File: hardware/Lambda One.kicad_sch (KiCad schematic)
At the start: 20 parts, among them IC1 01, J1 Conn_01x02, SW1 SW_Push, U1 W65C816SxP, U3 ATF22V10C, U6 74AHC1G04, Y1 TFT680

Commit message: Fixed some erros, changed to 3V
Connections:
- net +3.3V: now also IC1.2 (VCC), J1.2 (Pin_2), U1.8 (VDD), U3.24 (VCC), Y1.14 (Vcc)
- net +5V: no longer IC1.2 (VCC), J1.2 (Pin_2), U1.8 (VDD), U3.24 (VCC), Y1.14 (Vcc)

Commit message: Fixed all erros and warning
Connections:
- net +5V is gone; now on net +3.3V: R17.2, Y1.1 (EN)
- net IRQ_{1} renamed ~{IRQ}

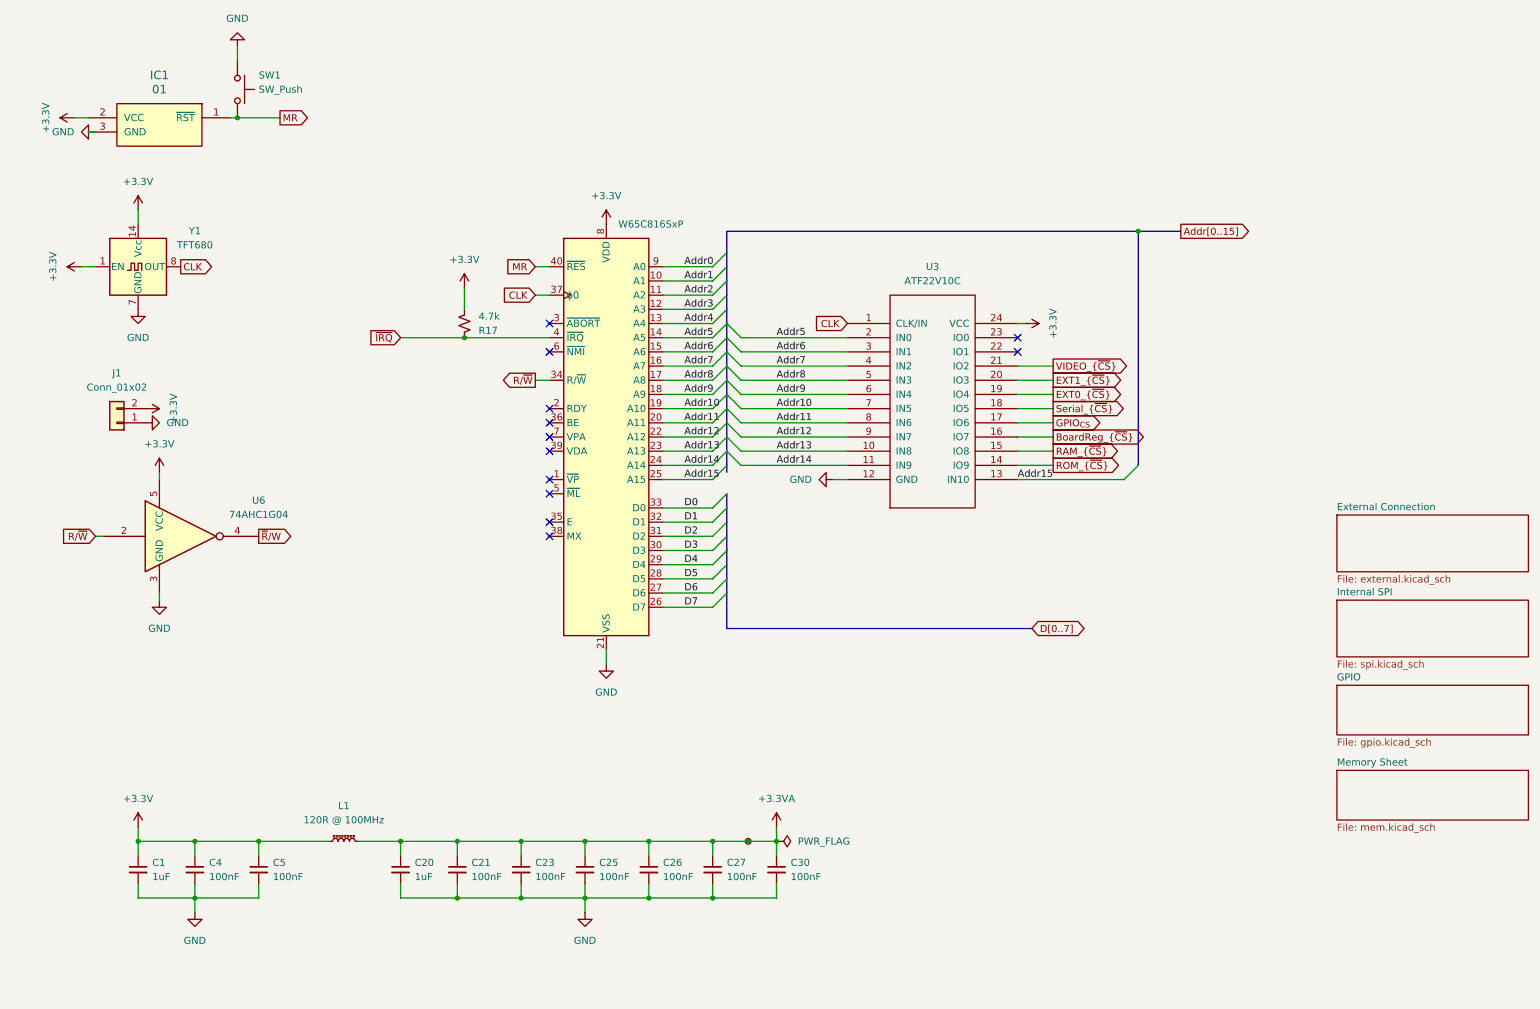
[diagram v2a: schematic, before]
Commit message: Fixed critical bugs on the system related to memory maping and IC selections
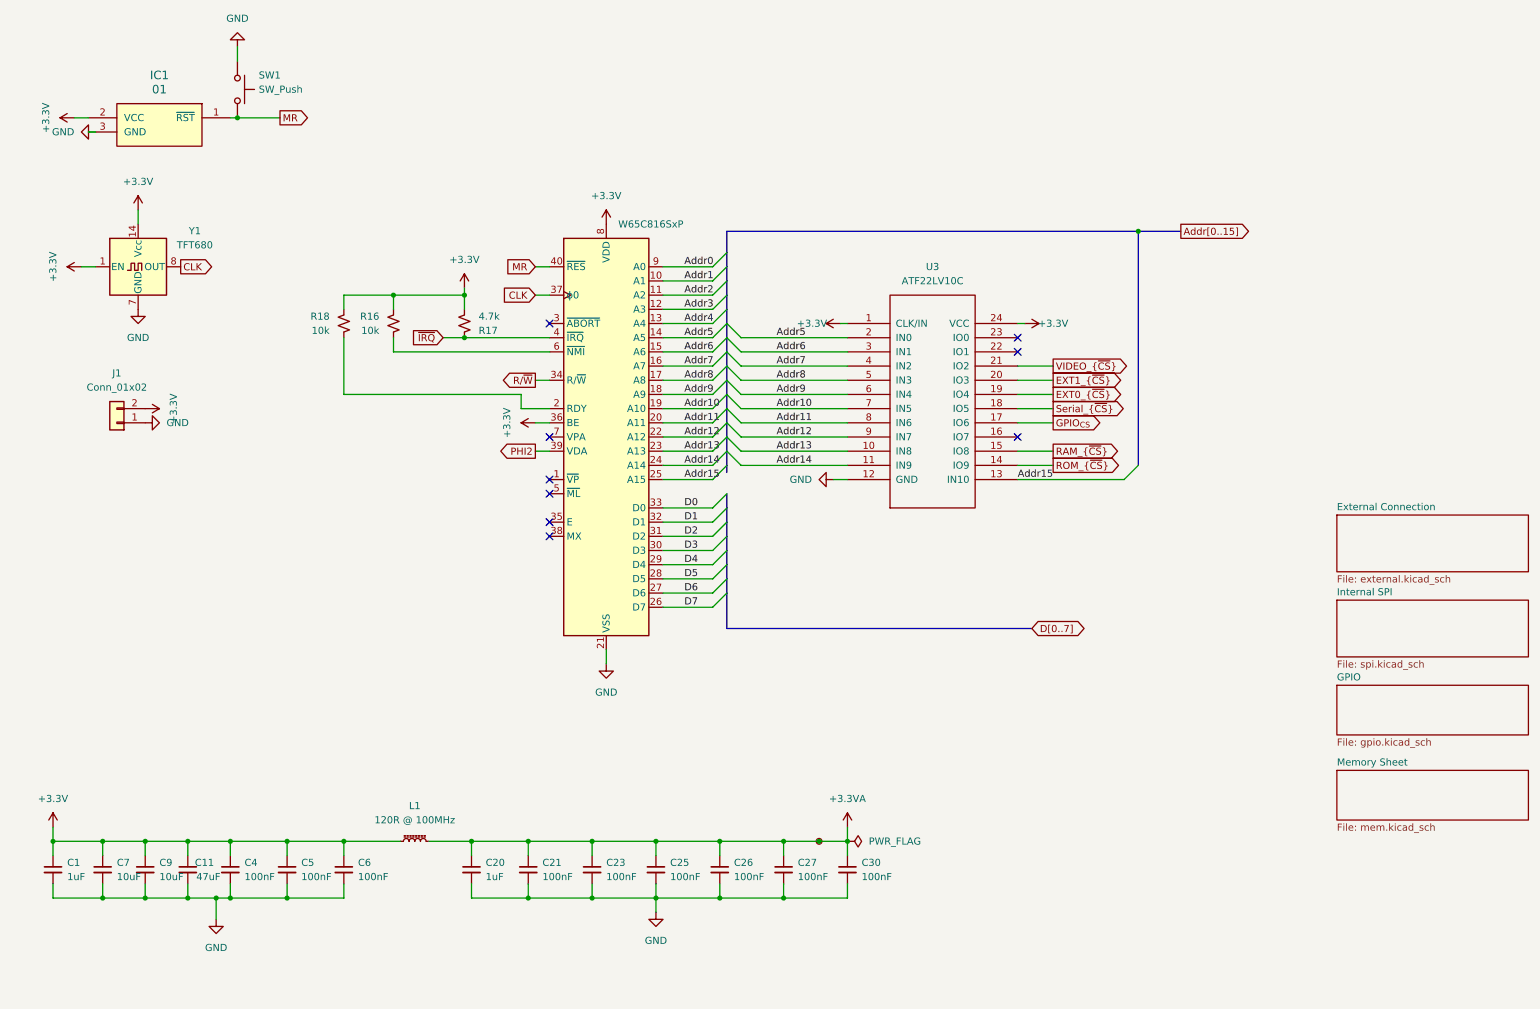
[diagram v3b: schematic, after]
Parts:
- removed U6: 74AHC1G04, Package_TO_SOT_SMD:SOT-23-5, symbol 74xGxx:74AHC1G04
- added C11: 47uF, Capacitor_SMD:C_0603_1608Metric, symbol Device:C_Small
- added C6: 100nF, Capacitor_SMD:C_0603_1608Metric, symbol Device:C_Small
- added C7, C9: 10uF, Capacitor_SMD:C_0603_1608Metric, symbol Device:C_Small
- added R16, R18: 10k, Resistor_SMD:R_0603_1608Metric, symbol Device:R_Small_US
- U3: value ATF22V10C -> ATF22LV10C
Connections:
- net +3.3V: now also U1.36 (BE), U3.1 (CLK/IN), C11.1, C6.1, C7.1, C9.1, R16.1, R18.1
- net CLK: no longer U3.1 (CLK/IN)
- net GND: now also C11.2, C6.2, C7.2, C9.2
- net at U1.2 (RDY): now also R18.2
- net PHI2: now reaches U1.39 (VDA)
- net at U1.6 (~{NMI}): now also R16.2
- net BoardReg_{~{CS}}: no longer names the net of U3.16 (IO7)
- no-connect marks 12 -> 9
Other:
- moved on the sheet: C1, C20, C21, C23, C25, C26, C27, C30, C4, C5, L1

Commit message: Changed Ethernet Chip to Ethernet ModuleWIZ850IO
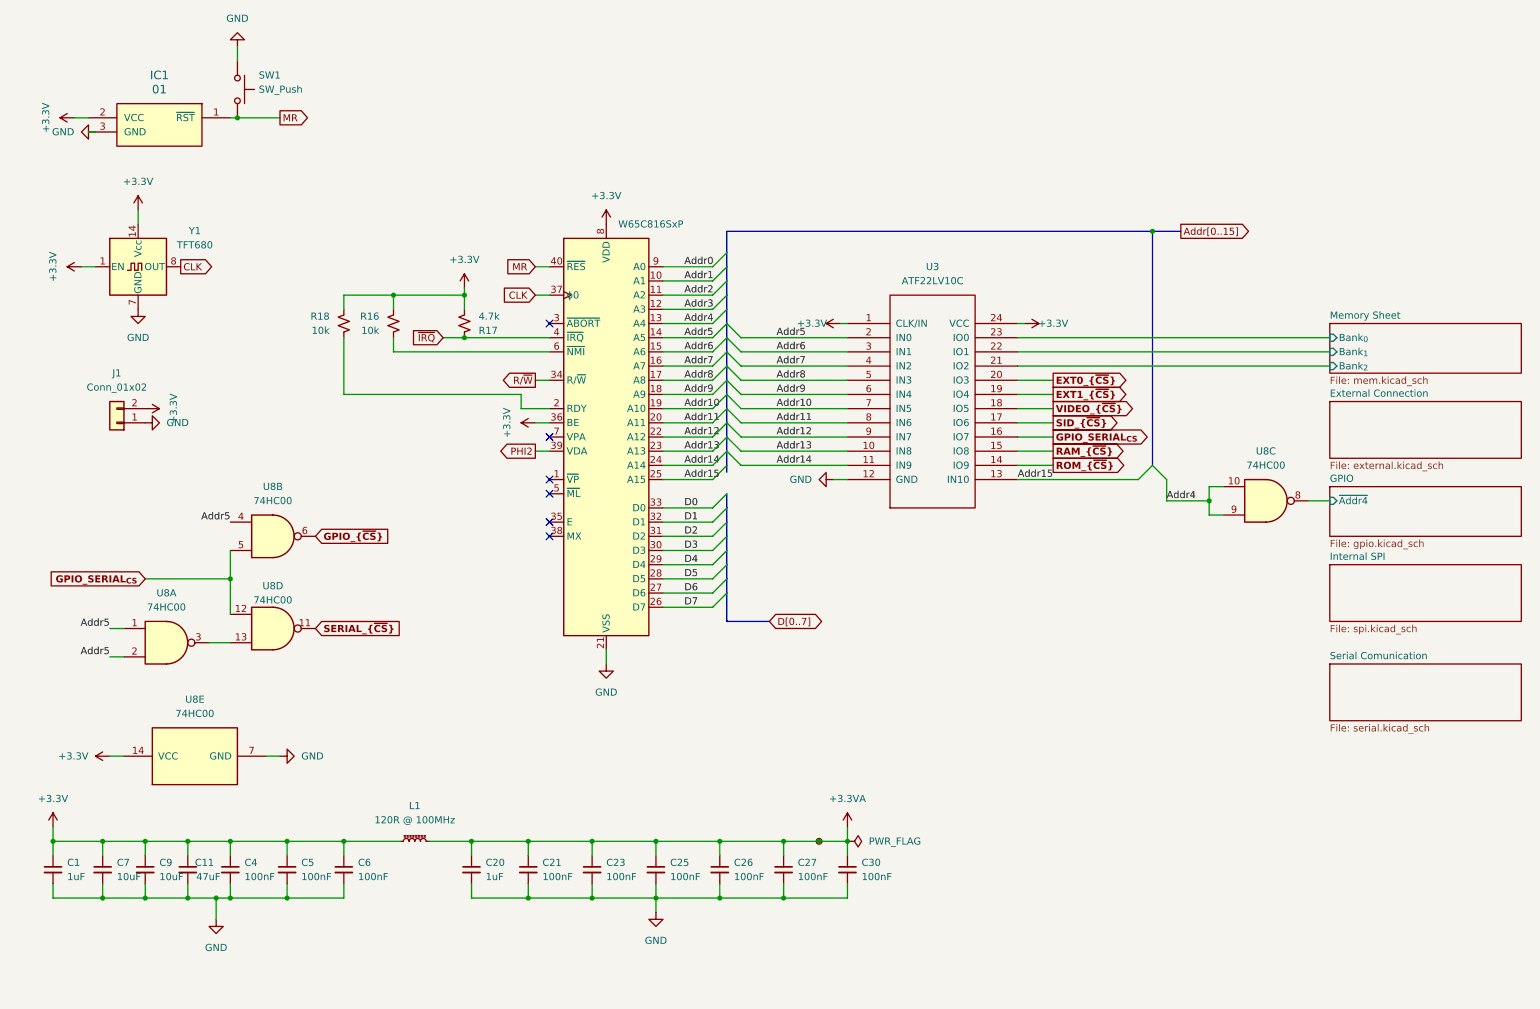
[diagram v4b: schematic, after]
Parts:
- added U8: 74HC00, symbol 74xx:74HC00
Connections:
- net Serial_{~{CS}} is gone; now on net VIDEO_{~{CS}}: U3.18 (IO5)
- net +3.3V: now also U8.14 (VCC)
- net Addr4: now also U8.10, U8.9
- net Addr5: now also U8.1, U8.2, U8.4
- net EXT0_{~{CS}}: now also U3.20 (IO3); no longer U3.19 (IO4)
- net EXT1_{~{CS}}: now also U3.19 (IO4); no longer U3.20 (IO3)
- net GND: now also U8.7 (GND)
- net VIDEO_{~{CS}}: no longer U3.21 (IO2)
- net GPIO_SERIAL_{CS}: now reaches U3.16 (IO7)
- net GPIO_SERIAL_{CS}: now also U8.12, U8.5
- net Memory Sheet/Bank_{1}: now reaches U3.22 (IO1)
- net Memory Sheet/Bank_{0}: now reaches U3.23 (IO0)
- net GPIO_{CS} renamed SID_{~{CS}}
- new net: U8.13, U8.3
- new net GPIO/~{Addr4}: U8.8
- new net GPIO_{~{CS}}: U8.6
- new net Memory Sheet/Bank_{2}: U3.21 (IO2)
- new net SERIAL_{~{CS}}: U8.11
- no-connect marks 9 -> 6
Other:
- added sheet Serial Comunication (serial.kicad_sch)
- sheet GPIO ports: added ~{Addr4}; removed none
- sheet Memory Sheet ports: added Bank_{0}, Bank_{1}, Bank_{2}; removed none

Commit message: Fixes and addres fix adding VDA AND VPA
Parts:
- removed C26, C27, C30: 100nF, Capacitor_SMD:C_0603_1608Metric, symbol Device:C_Small
- removed L1: 120R @ 100MHz, Inductor_SMD:L_0603_1608Metric, symbol Device:L_Ferrite_Small
- removed TP13: TestPoint_Small, TestPoint:TestPoint_Pad_D1.5mm, symbol Connector:TestPoint_Small
- added C2: 47uF, Capacitor_SMD:C_0603_1608Metric, symbol Device:C_Small
- added U9: 74HC00, symbol 74xx:74HC00
- IC1: value 01 -> DS1818
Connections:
- net +3.3VA is gone; now on net +3.3V: C20.1, C21.1, C23.1, C25.1
- net +3.3V: now also C2.1, U9.14 (VCC); no longer U3.1 (CLK/IN)
- net GND: now also C2.2, U9.7 (GND)
- net at U1.7 (VPA): now also U9.1, U9.2
- net PHI2: no longer names the net of U1.39 (VDA)
- net PHI2: now also U9.10, U9.9
- new net: U9.4, U9.8
- new net: U9.3, U9.5
- new net VDA&VPA: U3.1 (CLK/IN), U9.6
- no-connect marks 6 -> 8
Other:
- moved on the sheet: C1, C11, C20, C21, C23, C25, C4, C5, C6, C7, C9, R16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

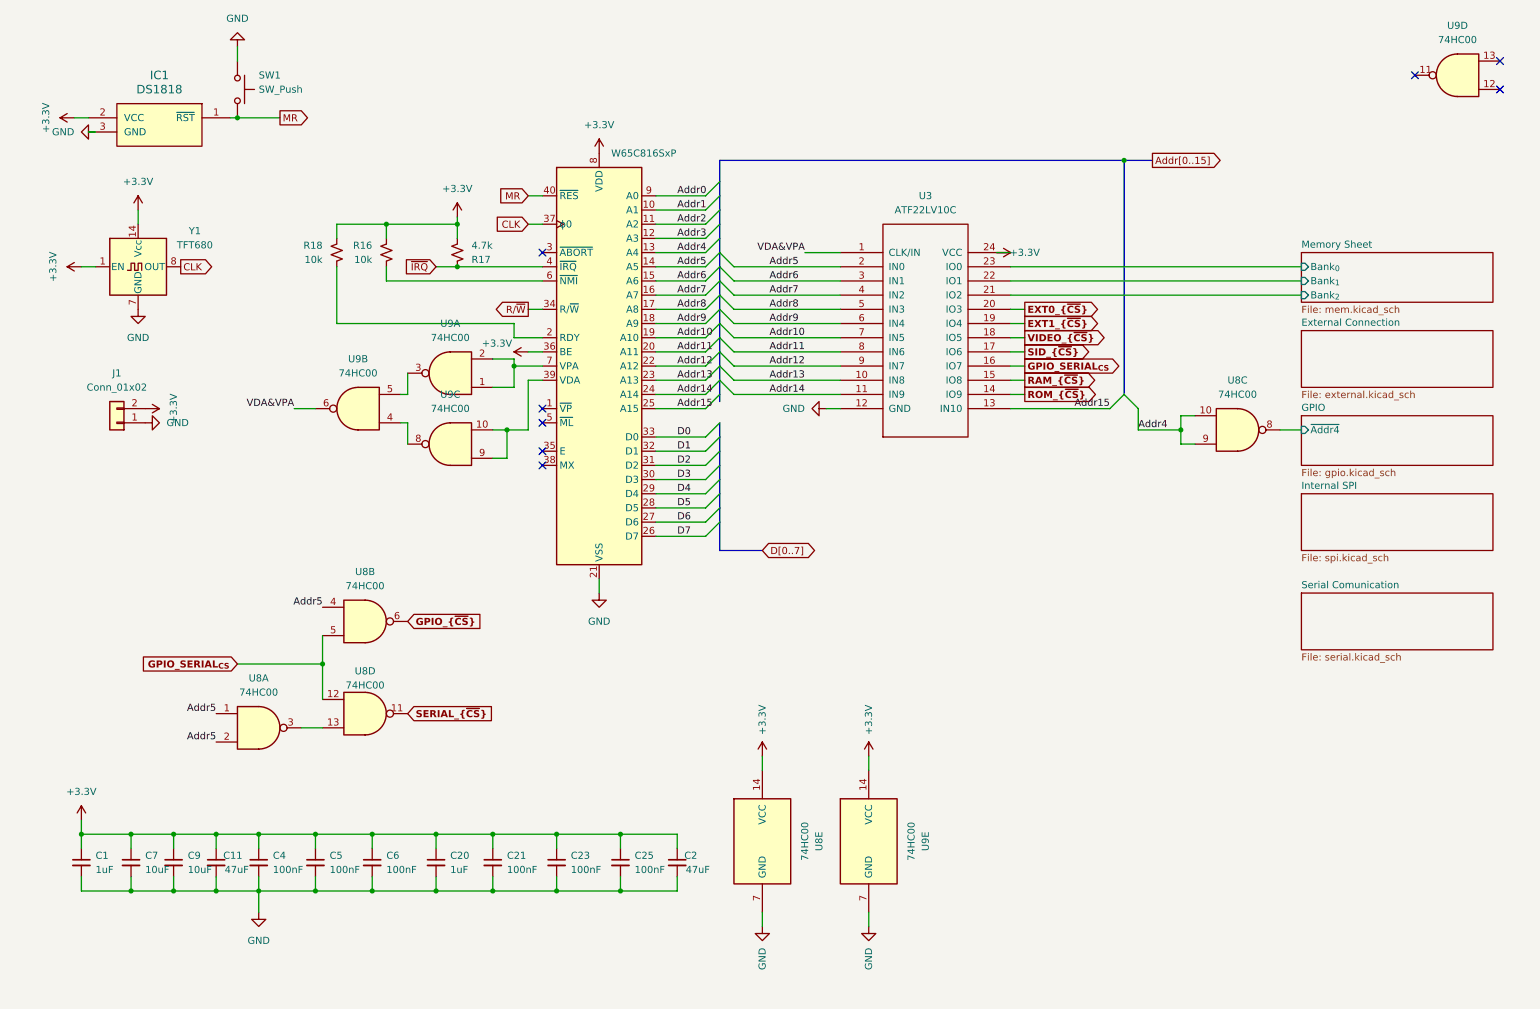
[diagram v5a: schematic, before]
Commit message: Added Bus controller 74HC245
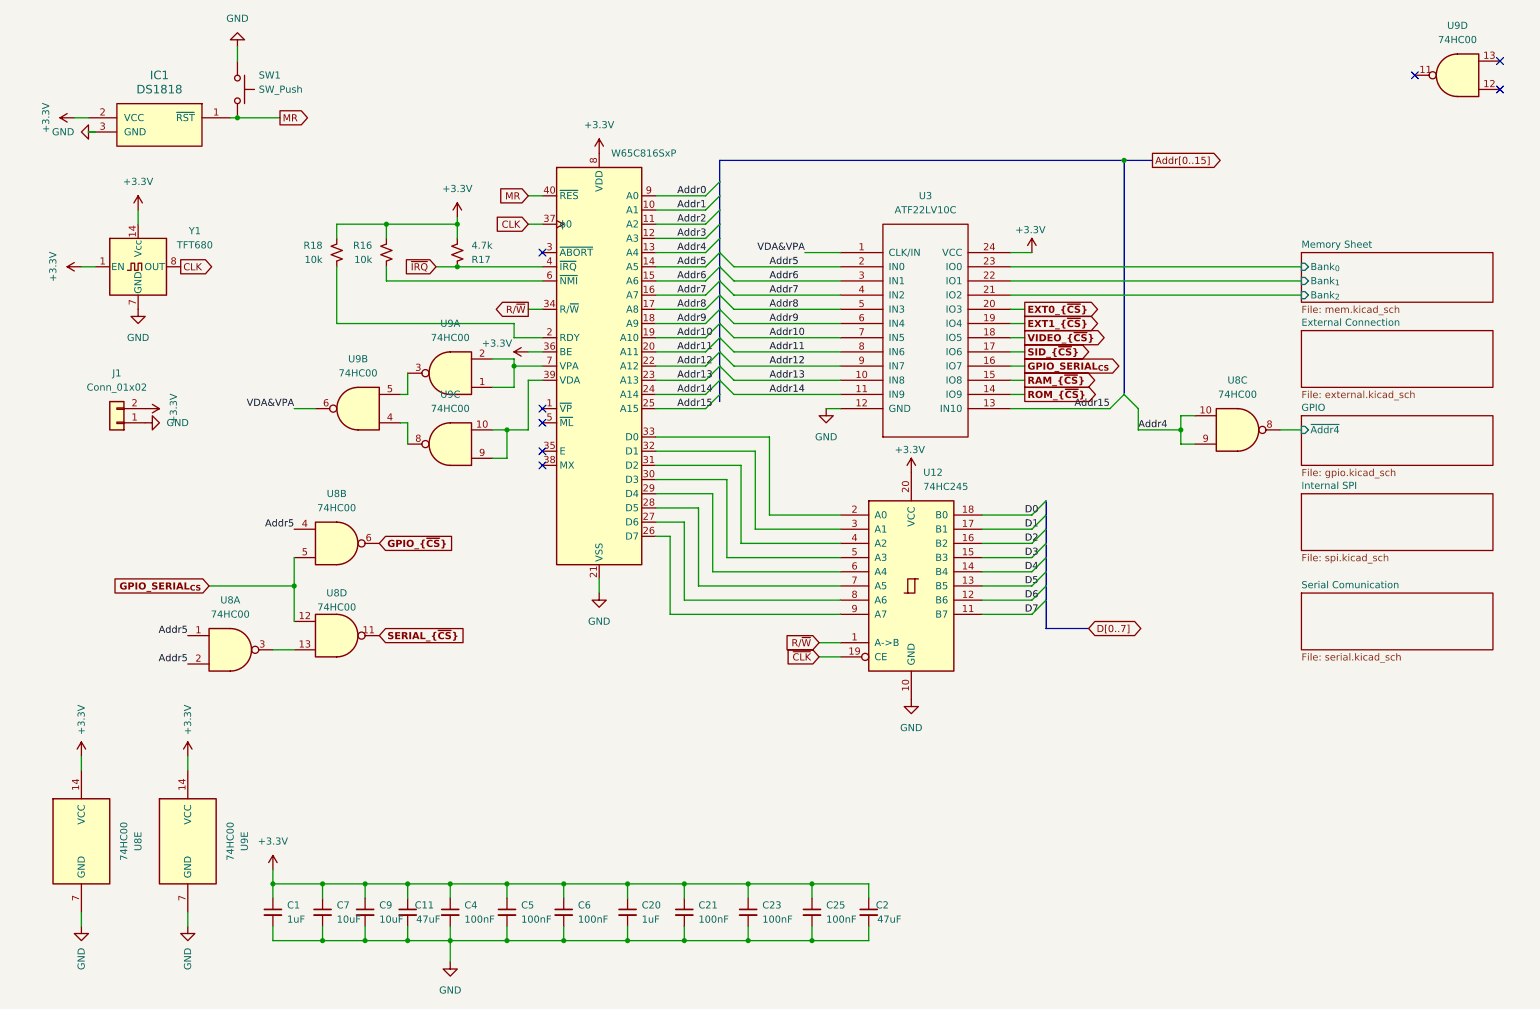
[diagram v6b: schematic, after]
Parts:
- added U12: 74HC245, Package_DIP:DIP-20_W7.62mm, symbol 74xx:74HC245
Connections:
- net +3.3V: now also U12.20 (VCC)
- net D0: now also U12.18 (B0); no longer U1.33 (D0)
- net D1: now also U12.17 (B1); no longer U1.32 (D1)
- net D2: now also U12.16 (B2); no longer U1.31 (D2)
- net D3: now also U12.15 (B3); no longer U1.30 (D3)
- net D4: now also U12.14 (B4); no longer U1.29 (D4)
- net D5: now also U12.13 (B5); no longer U1.28 (D5)
- net D6: now also U12.12 (B6); no longer U1.27 (D6)
- net D7: now also U12.11 (B7); no longer U1.26 (D7)
- net GND: now also U12.10 (GND)
- net R/~{W}: now also U12.1 (A->B)
- new net: U1.33 (D0), U12.2 (A0)
- new net: U1.32 (D1), U12.3 (A1)
- new net: U1.31 (D2), U12.4 (A2)
- new net: U1.30 (D3), U12.5 (A3)
- new net: U1.29 (D4), U12.6 (A4)
- new net: U1.28 (D5), U12.7 (A5)
- new net: U1.27 (D6), U12.8 (A6)
- new net: U1.26 (D7), U12.9 (A7)
- new net ~{CLK}: U12.19 (CE)
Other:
- moved on the sheet: C1, C11, C2, C20, C21, C23, C25, C4, C5, C6, C7, C9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
